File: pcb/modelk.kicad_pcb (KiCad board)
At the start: 2 copper layers, 150 x 38 mm, 52 parts, among them J1 JST-PH connector, J2 Conn_01x20, J3 User exposed, J4 Conn_01x12, J5 Conn_01x04, J6 Conn_01x08, J7 Faston PCB mount, J8 Dupont for power profiling, SW1 SW_reset, U1 nice_nano, U2 74HC595, U3 74HC595, U4 74HC595

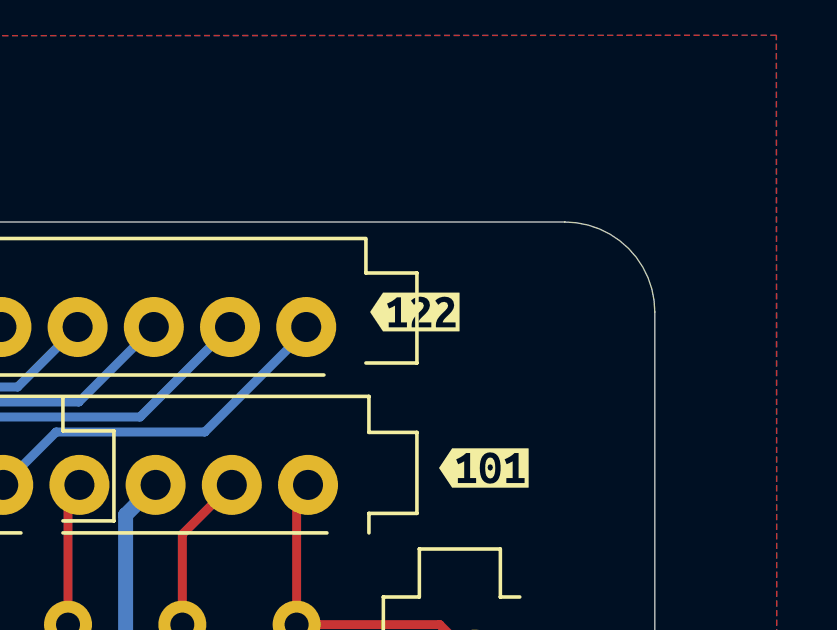
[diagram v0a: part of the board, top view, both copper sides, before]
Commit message: Made silkscreen not intersect
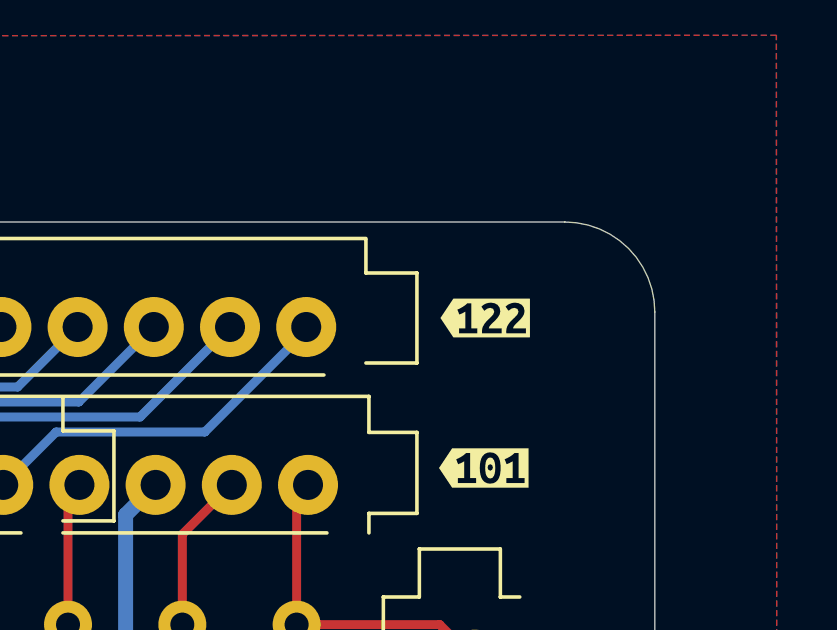
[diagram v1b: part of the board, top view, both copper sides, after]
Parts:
- moved kibuzzard-684FF5A3 2.35 mm to (209.1, 50.2)
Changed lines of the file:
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@@
 	(footprint "kibuzzard-684FF5A3"
 		(layer "F.Cu")
-		(at 206.770004 49.990006)
+		(at 209.115148 50.190006)
 		(descr "Generated with KiBuzzard")
 		(tags "kb_params=eyJBbGlnbm1lbnRDaG9pY2UiOiAiQ2VudGVyIiwgIkNhcExlZnRDaG9pY2UiOiAiPCIsICJDYXBSaWdodENob2ljZSI6ICJdIiwgIkZvbnRDb21ib0JveCI6ICJVYnVudHVNb25vLUIiLCAiSGVpZ2h0Q3RybCI6IDEuMCwgIkxheWVyQ29tYm9Cb3giOiAiRi5TaWxrUyIsICJMaW5lU3BhY2luZ0N0cmwiOiAxLjAsICJNdWx0aUxpbmVUZXh0IjogIjEyMiIsICJQYWRkaW5nQm90dG9tQ3RybCI6IDEuMCwgIlBhZGRpbmdMZWZ0Q3RybCI6IDEuMCwgIlBhZGRpbmdSaWdodEN0cmwiOiAxLjAsICJQYWRkaW5nVG9wQ3RybCI6IDEuMCwgIldpZHRoQ3RybCI6IDEuMCwgImFkdmFuY2VkQ2hlY2tib3giOiBmYWxzZSwgImlubGluZUZvcm1hdFRleHRib3giOiBmYWxzZSwgImxpbmVvdmVyU3R5bGVDaG9pY2UiOiAiU3F1YXJlIiwgImxpbmVvdmVyVGhpY2tuZXNzQ3RybCI6IDF9")

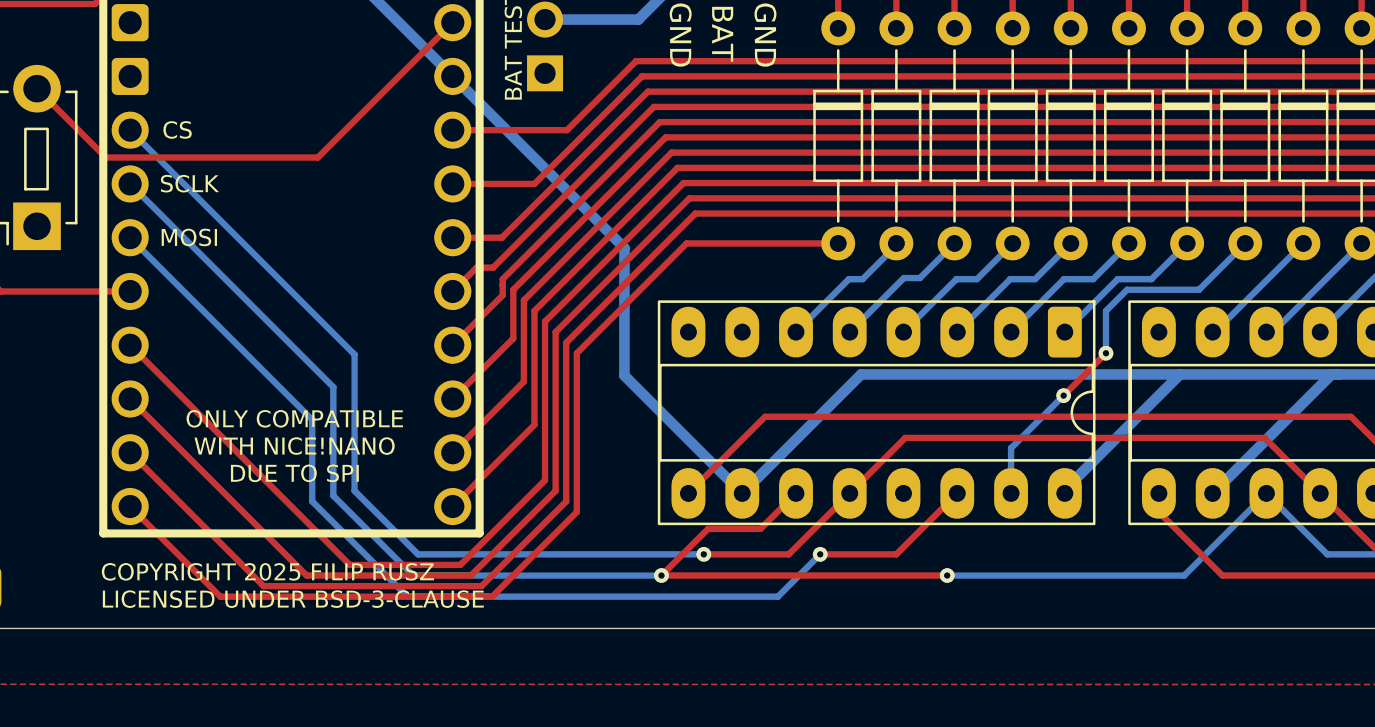
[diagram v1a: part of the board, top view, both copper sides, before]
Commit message: Spaced out signal tracks, less vias
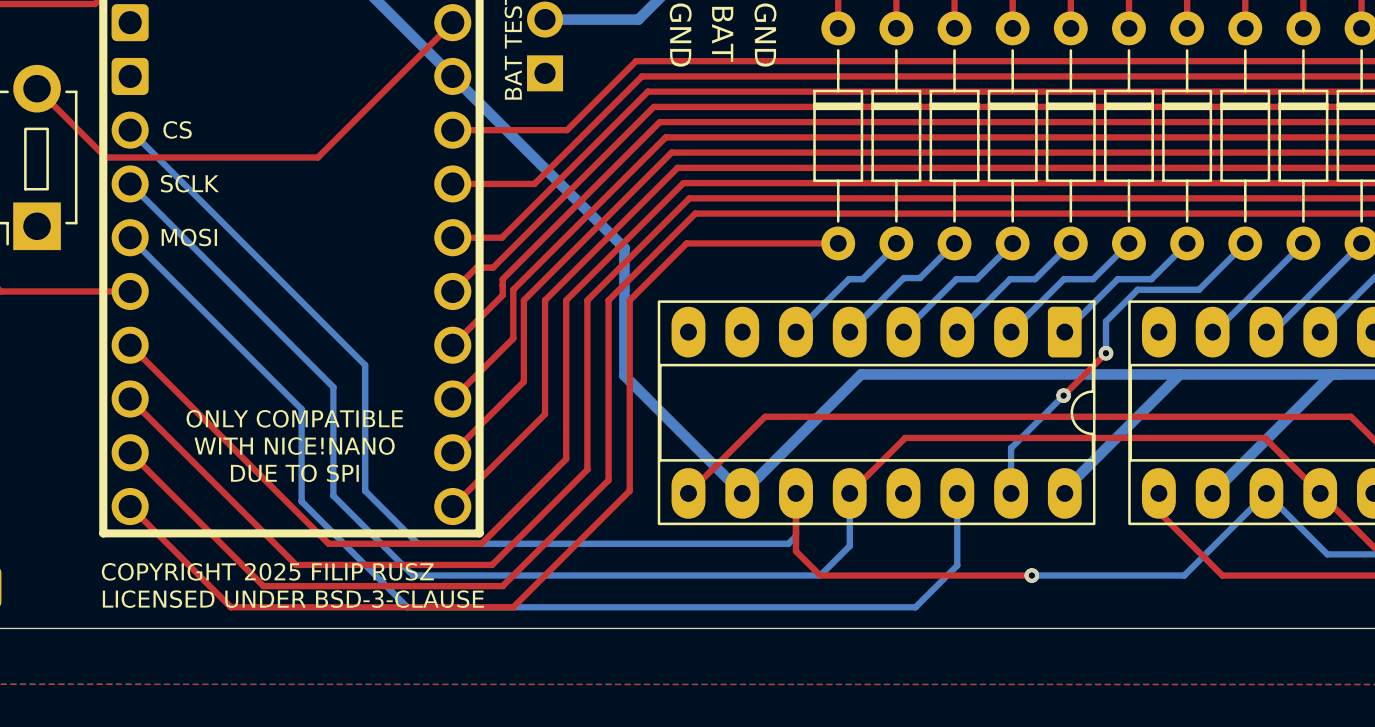
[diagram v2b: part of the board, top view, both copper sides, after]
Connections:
- U1 pad 6: CS -> SCLK
- U1 pad 7: SCLK -> CS
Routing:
- net MOSI: track 50.4 -> 53.1 mm, vias 1 -> 0
- net SCLK: track 99.3 -> 97.6 mm, vias 2 -> 1
- net col0: track 46.5 -> 47.8 mm
- net led2: track 140.6 -> 139.7 mm
- net CS: track 97.0 -> 97.7 mm, vias 1 -> 0
- net led0: track 130.5 -> 131.1 mm

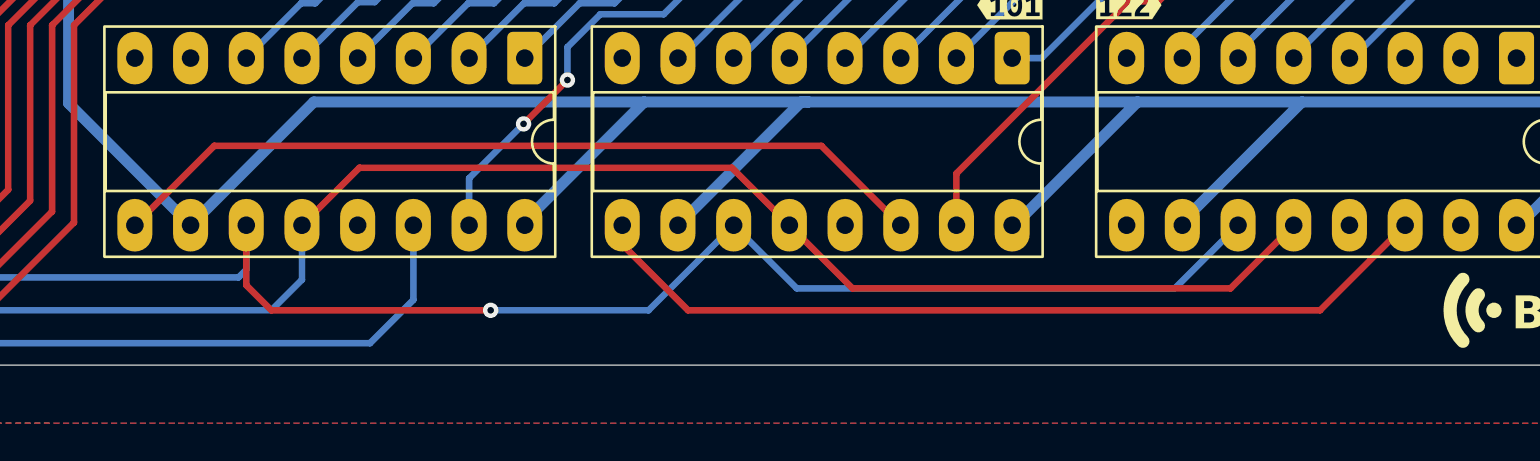
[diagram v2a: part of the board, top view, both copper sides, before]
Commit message: One less via
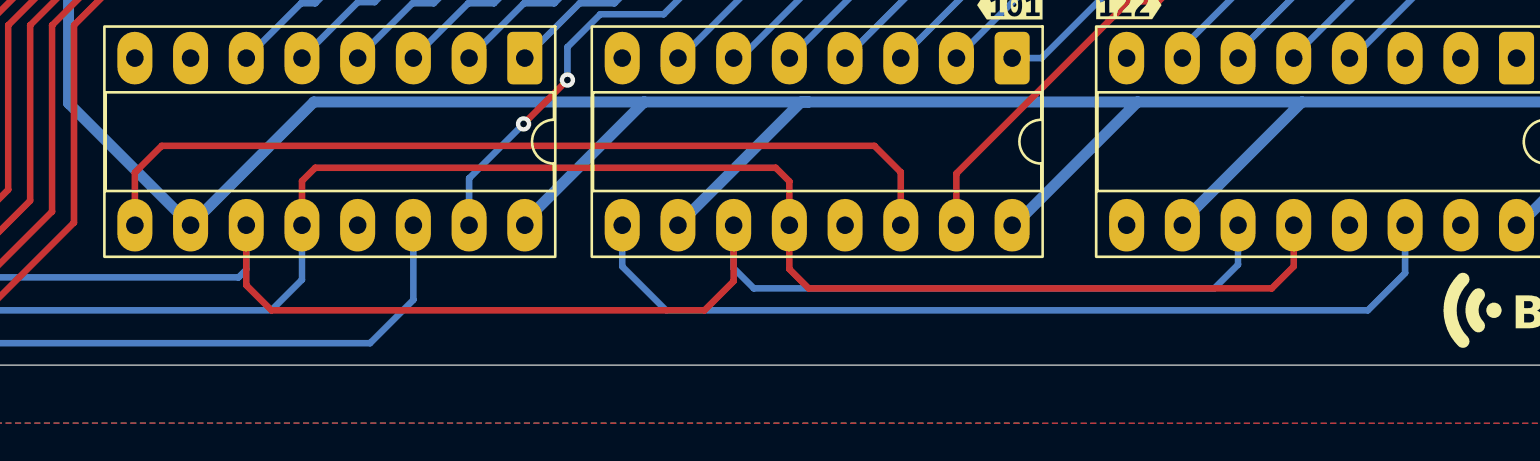
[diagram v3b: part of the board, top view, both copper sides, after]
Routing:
- net CS: track 97.7 -> 102.3 mm
- net SCLK: track 97.6 -> 101.3 mm, vias 1 -> 0
- net Net-(U2-QH'): track 37.9 -> 40.7 mm
- net Net-(U3-QH'): track 39.4 -> 41.3 mm

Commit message: Fixed DRC
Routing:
- net GND: track 0.00 -> 8.00 mm, vias 0 -> 3
